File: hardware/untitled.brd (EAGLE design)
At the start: 160 x 100 mm, 39 parts, among them J1 AUDIO_JACK_TRRSSMD_RA, U1 AT32UC3A1512/1256/1128, U2 USD-SOCKETUSD, Y2 CRYSTAL-GROUNDEDSMD-5X3.2

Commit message: PCB updated
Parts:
- added C10, C8: 22 pF, rcl:C0603
- added C22, C9: 33n, rcl:C0402
- added J2: GT-USB-7010, GT-USB-7010:GT-USB-7010
- added R2: 10k, rcl:R0402
- added U$3, U$8: SMT3X6X3.5MM, mw:SMT3X6X3.5MM
- added Y1: CRYSTAL-GROUNDEDSMD-5X3.2, SparkFun-Clocks:CRYSTAL-SMD-5X3.2-4PAD
- C1: device rcl:SMC_B -> rcl:SMC_A
- C2, C3, C4, C5: value (none) -> 2n7
- C6, C7: value (none) -> 33n
- moved C1 79.0 mm to (35.4, 61.2), flipped to the bottom, turned to 90 degrees
- moved R40 75.6 mm to (38.5, 56.9), flipped to the bottom, turned to 90 degrees
- moved R39 68.0 mm to (34.6, 54.1)
- moved R1 67.6 mm to (34.6, 51.1)
- moved R53 66.5 mm to (36.6, 57.0)
- moved C29 64.9 mm to (38.7, 61.4)
- moved U2 64.9 mm to (37.5, 77.5)
- moved C5 64.6 mm to (23.8, 20.3)
- moved C11 64.3 mm to (1.91, 51.4)
- moved C12 64.3 mm to (1.91, 49.5)
- moved C13 64.3 mm to (10.7, 57.8)
- moved C14 64.3 mm to (8.23, 58.1)
- moved C15 64.3 mm to (22.2, 59.3)
- moved C16 64.3 mm to (20.3, 59.5)
- moved C17 64.3 mm to (26.6, 55.5)
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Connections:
- new net D_N: J2.A7, J2.B7, U1.48
- new net D_P: J2.A6, J2.B6, U1.49
- new net KEY_VOLUP: U$8.B, U1.26
- new net OSC_IN: C10.1, U1.85, Y1.1
- new net OSC_OUT: C8.1, U1.86, Y1.3
- new net VBUS: J2.A4B9, J2.B4A9, U1.46
- net 3V: now also R2.2
- net GND: now also C10.2, C22.2, C8.2, C9.2, J2.A1B12, J2.B1A12, U$8.A, U$8.MNT1, U$8.MNT2, Y1.2, Y1.4
- net MOSI: now also R2.1
- net VDDCORE: now also C22.1, C9.1
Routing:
- net 3V: track 48.2 -> 95.8 mm, vias 2 -> 4
- net KEY_VOLUP: track 0.00 -> 29.3 mm
- net OSC_OUT: track 0.00 -> 7.92 mm
- net OSC_IN: track 0.00 -> 7.91 mm
- net I2C1_SDA: track 37.3 -> 30.0 mm
- net I2C1_SCL: track 35.0 -> 28.6 mm
- net D_N: track 0.00 -> 6.07 mm
- net VDDCORE: track 57.1 -> 62.5 mm
- net D_P: track 0.00 -> 5.29 mm
- net GND: track 19.1 -> 23.9 mm
- net N$1: track 25.3 -> 21.2 mm
- net SD_CS: track 32.9 -> 37.0 mm
- net SCK: track 9.99 -> 13.8 mm
- net MISO: track 35.0 -> 34.3 mm
- net SD_PRESENT: track 36.2 -> 36.4 mm, vias 0 -> 1
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- added copper zone on layer 16, net AGND
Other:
- board size 160 x 100 mm -> 47 x 77.8 mm

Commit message: PCB updated
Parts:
- removed J2: GT-USB-7010, GT-USB-7010:GT-USB-7010
- added C27: 2n7, rcl:C0402
- added C28: 33n, rcl:C0402
- added R3, R4, R7: (no value), rcl:R0402
- added U$4: MICRO-USBV2, microusb:MICRO-USB-2
- R15: device rcl:R0603 -> rcl:R0402
- moved C20 1.82 mm to (9.80, 49.0), turned to 180 degrees
- moved R15 0.99 mm to (14.3, 45.6)
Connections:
- new net D_P_1: R7.2, U$4.3
- new net N$4: R4.2, U$4.2
- net 3V: now also C27.1, C28.1, R3.2
- net D_N: now also R4.1; no longer J2.A7, J2.B7
- net D_P: now also R7.1; no longer J2.A6, J2.B6
- net GND: now also C27.2, C28.2, U$4.5, U$4.P$1, U$4.P$2, U$4.P$3, U$4.P$4; no longer J2.A1B12, J2.B1A12
- net I2C1_SDA: now also R3.1
- net VBUS: now also U$4.1; no longer J2.A4B9, J2.B4A9
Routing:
- net VBUS: track 0.00 -> 17.2 mm, vias 0 -> 2
- net GND: track 23.9 -> 27.2 mm, vias 5 -> 7
- net I2C1_SDA: track 30.0 -> 33.1 mm
- net N$4: track 0.00 -> 2.46 mm
- net D_P_1: track 0.00 -> 2.46 mm
- net D_P: track 5.29 -> 6.43 mm
- net D_N: track 6.07 -> 7.20 mm
- net 3V: track 95.8 -> 96.6 mm

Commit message: PCB updated
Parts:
- added C30, C32: 33n, rcl:C0402
- added C31, C33: 100n, rcl:C0402
- C27: value 2n7 -> 33n
- C28: value 33n -> 100n
- moved Y1 3.18 mm to (18.1, 17.4)
- moved C10 3.17 mm to (16.8, 14.0)
- moved C8 3.17 mm to (19.3, 14.0)
- moved R40 0.07 mm to (38.6, 56.9)
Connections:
- net 3V: now also C30.1, C31.1, C32.1, C33.1
- net GND: now also C30.2, C31.2, C32.2, C33.2
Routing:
- net 3V: track 96.6 -> 104.5 mm
- net GND: track 27.2 -> 31.2 mm, vias 7 -> 8
- net OSC_OUT: track 7.92 -> 11.1 mm
- net OSC_IN: track 7.91 -> 11.1 mm
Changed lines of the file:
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@@
 <element name="R39" library="rcl" package="R0603" value="10k" x="34.56" y="54.1274"/>
 <element name="C29" library="rcl" package="C0603" value="100n" x="38.6588" y="61.3664"/>
-<element name="R40" library="rcl" package="R0603" value="10k" x="38.489" y="56.896" rot="MR90"/>
+<element name="R40" library="rcl" package="R0603" value="10k" x="38.5572" y="56.896" rot="MR90"/>
 <element name="C1" library="rcl" package="SMC_A" value="" x="35.3822" y="61.1632" rot="MR90"/>
 <element name="R53" library="rcl" package="R0603" value="10k" x="36.576" y="56.9976" rot="R180"/>
@@
 <element name="C6" library="rcl" package="C0402" value="33n" x="20.955" y="45.8978" rot="R90"/>
 <element name="C7" library="rcl" package="C0402" value="33n" x="25.4" y="44.069" rot="R90"/>
-<element name="C8" library="rcl" package="C0603" value="22 pF" x="19.34845" y="17.145" rot="R270"/>
-<element name="C10" library="rcl" package="C0603" value="22 pF" x="16.80845" y="17.145" rot="R270"/>
-<element name="Y1" library="SparkFun-Clocks" package="CRYSTAL-SMD-5X3.2-4PAD" value="CRYSTAL-GROUNDEDSMD-5X3.2" x="18.07845" y="20.6248"/>
+<element name="C8" library="rcl" package="C0603" value="22 pF" x="19.34845" y="13.97" rot="R270"/>
+<element name="C10" library="rcl" package="C0603" value="22 pF" x="16.80845" y="13.97" rot="R270"/>
+<element name="Y1" library="SparkFun-Clocks" package="CRYSTAL-SMD-5X3.2-4PAD" value="CRYSTAL-GROUNDEDSMD-5X3.2" x="18.07845" y="17.4498"/>
 <element name="C9" library="rcl" package="C0402" value="33n" x="30.4038" y="37.5412"/>
 <element name="C22" library="rcl" package="C0402" value="33n" x="25.146" y="20.32" rot="R270"/>
@@
 <element name="U$4" library="microusb" package="MICRO-USB-2" value="MICRO-USBV2" x="0" y="41.275" rot="R270"/>
 <element name="R7" library="rcl" package="R0402" value="" x="8.255" y="40.9575" rot="R180"/>
-<element name="C27" library="rcl" package="C0402" value="2n7" x="13.1318" y="42.7482" rot="R180"/>
-<element name="C28" library="rcl" package="C0402" value="33n" x="13.1318" y="44.069" rot="R180"/>
+<element name="C27" library="rcl" package="C0402" value="33n" x="13.1318" y="42.7482" rot="R180"/>
+<element name="C28" library="rcl" package="C0402" value="100n" x="13.1318" y="44.069" rot="R180"/>
 <element name="R3" library="rcl" package="R0402" value="" x="15.5702" y="42.7482" rot="R180"/>
+<element name="C30" library="rcl" package="C0402" value="33n" x="15.67688125" y="21.59"/>
+<element name="C31" library="rcl" package="C0402" value="100n" x="15.67688125" y="20.2692"/>
+<element name="C32" library="rcl" package="C0402" value="33n" x="8.89" y="28.450540625" rot="R270"/>
+<element name="C33" library="rcl" package="C0402" value="100n" x="7.5692" y="28.450540625" rot="R270"/>
 </elements>
 <signals>
@@
 <wire x1="5.275" y1="39.975" x2="6.1676" y2="39.975" width="0.4064" layer="1"/>
 <wire x1="6.1676" y1="39.975" x2="6.2484" y2="40.0558" width="0.4064" layer="1"/>
+<contactref element="C30" pad="2"/>
+<contactref element="C31" pad="2"/>
+<wire x1="15.3294" y1="23.8008" x2="15.3294" y2="22.7452" width="0.3048" layer="1"/>
+<wire x1="15.3294" y1="22.7452" x2="15.7988" y2="22.2758" width="0.3048" layer="1"/>
+<wire x1="15.7988" y1="22.2758" x2="16.2814" y2="22.2758" width="0.3048" layer="1"/>
+<wire x1="16.2814" y1="22.2758" x2="16.3068" y2="22.2504" width="0.3048" layer="1"/>
+<via x="14.3256" y="18.4404" extent="1-16" drill="0.6" diameter="1.4224" shape="octagon"/>
+<contactref element="C32" pad="2"/>
+<contactref element="C33" pad="2"/>
+<wire x1="11.3294" y1="28.8008" x2="10.081" y2="28.8008" width="0.3048" layer="1"/>
+<wire x1="10.081" y1="28.8008" x2="9.7028" y2="28.4226" width="0.3048" layer="1"/>
 <wire x1="27.3294" y1="27.8008" x2="27.3294" y2="31.8008" width="0" layer="19" extent="1-1"/>
 <wire x1="27.3294" y1="35.8008" x2="27.3294" y2="31.8008" width="0" layer="19" extent="1-1"/>
-<wire x1="15.3294" y1="23.8008" x2="16.22845" y2="21.7748" width="0" layer="19" extent="1-1"/>
-<wire x1="11.3294" y1="28.8008" x2="15.3294" y2="23.8008" width="0" layer="19" extent="1-1"/>
+<wire x1="9.7028" y1="28.4226" x2="8.89" y2="27.800540625" width="0" layer="19" extent="1-1"/>
 <wire x1="11.3294" y1="32.8008" x2="11.3294" y2="28.8008" width="0" layer="19" extent="1-1"/>
 </signal>
@@
 <wire x1="30.7848" y1="56.8198" x2="33.6282" y2="59.6632" width="0.8128" layer="16"/>
 <wire x1="35.3822" y1="59.6632" x2="33.6282" y2="59.6632" width="0.8128" layer="16"/>
-<wire x1="38.489" y1="57.746" x2="38.489" y2="58.7392" width="0.6096" layer="16"/>
-<wire x1="38.489" y1="58.7392" x2="37.5666" y2="59.6616" width="0.6096" layer="16"/>
 <contactref element="C27" pad="1"/>
 <contactref element="U1" pad="68"/>
@@
 <wire x1="13.7818" y1="42.7482" x2="14.9202" y2="42.7482" width="0.6096" layer="1"/>
 <wire x1="14.8294" y1="42.6574" x2="14.9202" y2="42.7482" width="0.3048" layer="1"/>
+<contactref element="C31" pad="1"/>
+<contactref element="C30" pad="1"/>
+<wire x1="14.8294" y1="23.8008" x2="14.8294" y2="21.59" width="0.3048" layer="1"/>
+<wire x1="14.8294" y1="21.59" x2="14.8294" y2="20.46668125" width="0.3048" layer="1"/>
+<wire x1="14.8294" y1="20.46668125" x2="15.02688125" y2="20.2692" width="0.3048" layer="1"/>
+<wire x1="15.02688125" y1="21.59" x2="14.8294" y2="21.59" width="0.3048" layer="1"/>
+<contactref element="C33" pad="1"/>
+<contactref element="C32" pad="1"/>
+<wire x1="11.3294" y1="29.3008" x2="8.89" y2="29.3008" width="0.3048" layer="1"/>
+<wire x1="8.89" y1="29.3008" x2="7.769459375" y2="29.3008" width="0.3048" layer="1"/>
+<wire x1="7.769459375" y1="29.3008" x2="7.5692" y2="29.100540625" width="0.3048" layer="1"/>
+<wire x1="8.89" y1="29.100540625" x2="8.89" y2="29.3008" width="0.3048" layer="1"/>
+<wire x1="38.5572" y1="57.746" x2="38.5572" y2="58.671" width="0.6096" layer="16"/>
+<wire x1="38.5572" y1="58.671" x2="37.5666" y2="59.6616" width="0.6096" layer="16"/>
 <wire x1="27.3294" y1="27.3008" x2="27.3294" y2="31.3008" width="0" layer="19" extent="1-1"/>
 <wire x1="33.02" y1="31.3008" x2="27.3294" y2="31.3008" width="0" layer="19" extent="1-1"/>
@@
 <wire x1="23.3294" y1="40.9316" x2="23.749" y2="41.3512" width="0.3048" layer="1"/>
 <wire x1="23.749" y1="41.3512" x2="29.0322" y2="41.3512" width="0.3048" layer="1"/>
-<via x="38.489" y="54.48" extent="1-16" drill="0.6" diameter="1.27" shape="octagon"/>
-<wire x1="29.0322" y1="41.3512" x2="38.489" y2="50.808" width="0.3048" layer="1"/>
-<wire x1="38.489" y1="54.48" x2="38.489" y2="50.808" width="0.3048" layer="1"/>
-<wire x1="38.489" y1="54.48" x2="38.489" y2="57.1834" width="0.3048" layer="1"/>
+<via x="38.5572" y="54.48" extent="1-16" drill="0.6" diameter="1.27" shape="octagon"/>
+<wire x1="29.0322" y1="41.3512" x2="38.5572" y2="50.8762" width="0.3048" layer="1"/>
 <wire x1="43.315" y1="63.22" x2="43.315" y2="62.0094" width="0.3048" layer="1"/>
-<wire x1="43.315" y1="62.0094" x2="38.489" y2="57.1834" width="0.3048" layer="1"/>
-<wire x1="38.489" y1="56.046" x2="38.489" y2="54.48" width="0.6096" layer="16"/>
+<wire x1="43.315" y1="62.0094" x2="38.5572" y2="57.2516" width="0.3048" layer="1"/>
+<wire x1="38.5572" y1="50.8762" x2="38.5572" y2="54.48" width="0.3048" layer="1"/>
+<wire x1="38.5572" y1="54.48" x2="38.5572" y2="57.2516" width="0.3048" layer="1"/>
+<wire x1="38.5572" y1="54.48" x2="38.5572" y2="56.046" width="0.6096" layer="16"/>
 </signal>
 <signal name="N$1">
@@
 <contactref element="Y1" pad="3"/>
 <contactref element="U1" pad="86"/>
-<wire x1="18.3294" y1="23.8008" x2="18.3294" y2="21.7748" width="0.3048" layer="1"/>
-<wire x1="18.3294" y1="21.7748" x2="18.3294" y2="18.8562" width="0.3048" layer="1"/>
-<wire x1="19.92845" y1="21.7748" x2="18.3294" y2="21.7748" width="0.3048" layer="1"/>
-<wire x1="18.3294" y1="18.8562" x2="19.1906" y2="17.995" width="0.3048" layer="1"/>
-<wire x1="19.34845" y1="17.995" x2="19.1906" y2="17.995" width="0.3048" layer="1"/>
+<wire x1="18.3294" y1="23.8008" x2="18.3294" y2="18.5998" width="0.3048" layer="1"/>
+<wire x1="18.3294" y1="18.5998" x2="18.3294" y2="15.6812" width="0.3048" layer="1"/>
+<wire x1="19.92845" y1="18.5998" x2="18.3294" y2="18.5998" width="0.3048" layer="1"/>
+<wire x1="18.3294" y1="15.6812" x2="19.1906" y2="14.82" width="0.3048" layer="1"/>
+<wire x1="19.34845" y1="14.82" x2="19.1906" y2="14.82" width="0.3048" layer="1"/>
 </signal>
 <signal name="OSC_IN">
@@
 <contactref element="Y1" pad="1"/>
 <contactref element="U1" pad="85"/>
-<wire x1="17.8294" y1="23.8008" x2="17.8294" y2="19.4748" width="0.3048" layer="1"/>
-<wire x1="17.8294" y1="19.4748" x2="17.8294" y2="18.8708" width="0.3048" layer="1"/>
-<wire x1="16.22845" y1="19.4748" x2="17.8294" y2="19.4748" width="0.3048" layer="1"/>
-<wire x1="17.8294" y1="18.8708" x2="16.9536" y2="17.995" width="0.3048" layer="1"/>
-<wire x1="16.80845" y1="17.995" x2="16.9536" y2="17.995" width="0.3048" layer="1"/>
+<wire x1="17.8294" y1="23.8008" x2="17.8294" y2="16.2998" width="0.3048" layer="1"/>
+<wire x1="17.8294" y1="16.2998" x2="17.8294" y2="15.6958" width="0.3048" layer="1"/>
+<wire x1="16.22845" y1="16.2998" x2="17.8294" y2="16.2998" width="0.3048" layer="1"/>
+<wire x1="17.8294" y1="15.6958" x2="16.9536" y2="14.82" width="0.3048" layer="1"/>
+<wire x1="16.80845" y1="14.82" x2="16.9536" y2="14.82" width="0.3048" layer="1"/>
 </signal>
 <signal name="KEY_VOLUP">

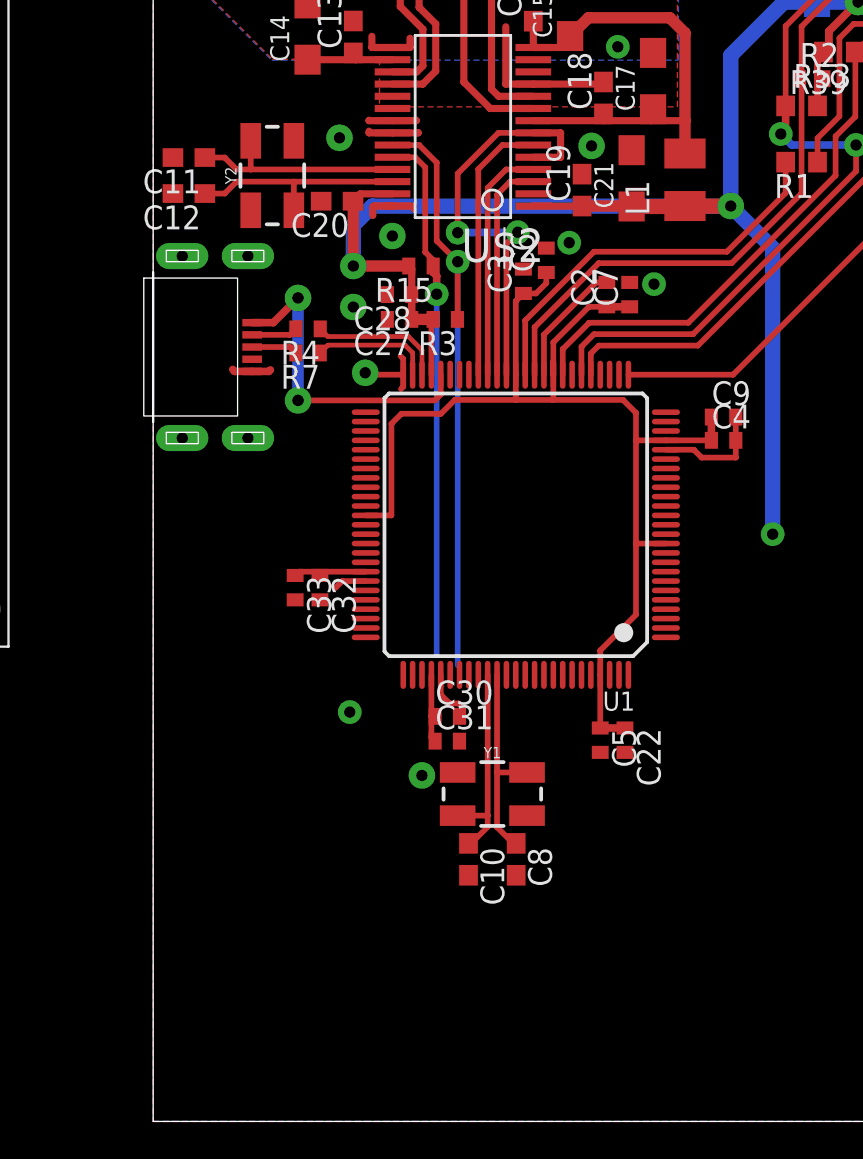
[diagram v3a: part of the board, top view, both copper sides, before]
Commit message: PCB update. USB-C instead of microUSB, PMIC (work in progress)
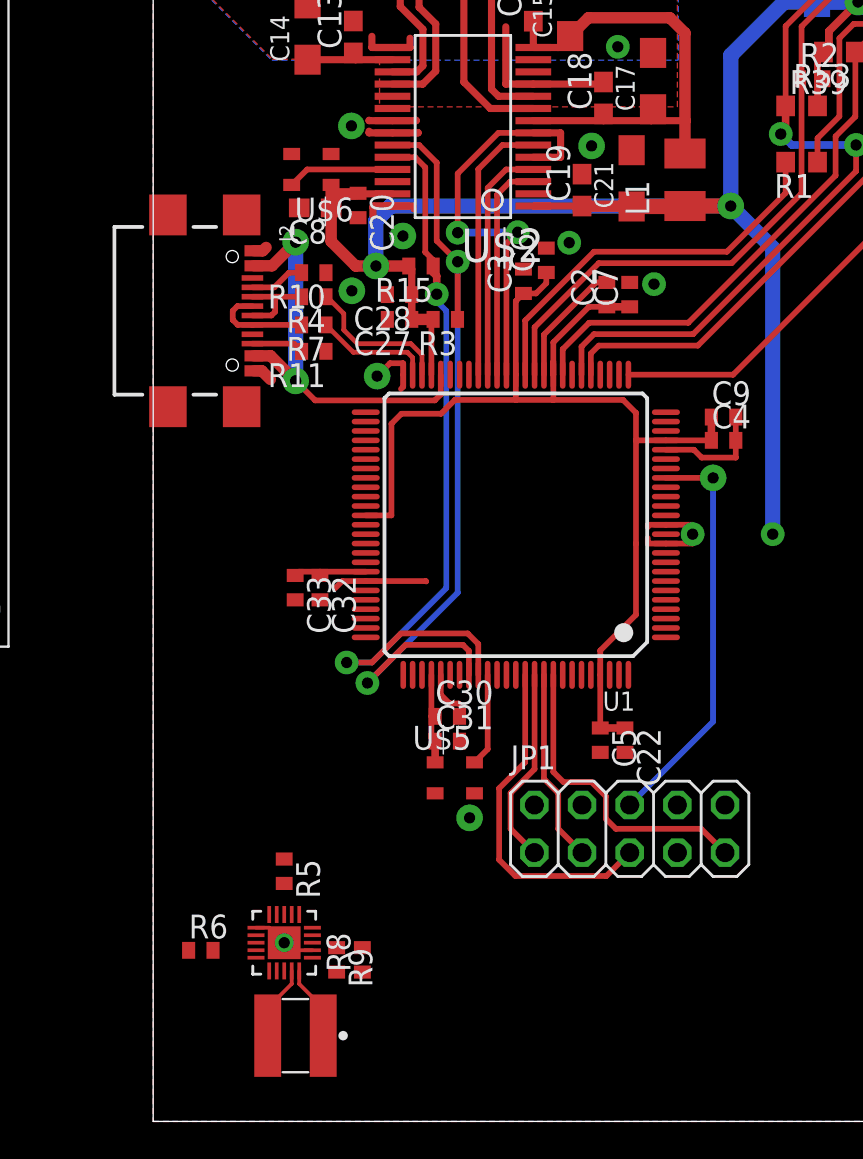
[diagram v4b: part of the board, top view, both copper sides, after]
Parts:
- removed C10, C11, C12: 22 pF, rcl:C0603
- removed U$4: MICRO-USBV2, microusb:MICRO-USB-2
- removed Y1, Y2: CRYSTAL-GROUNDEDSMD-5X3.2, SparkFun-Clocks:CRYSTAL-SMD-5X3.2-4PAD
- added J2: USB4110-GF-A, connector_tst:GCT_USB4110-GF-A
- added JP1: (no value), pinhead:2X05
- added L2: COILCRAFT-LPS4018, passives:LPS4018
- added R10, R11, R5, R6, R8, R9: (no value), rcl:R0402
- added U$5, U$6: ASE, crystal:ASE
- added U3: LTC3558EUDTRPBFQFN-20_UD_LIT-M, mw:QFN-20_UD_LIT-M
- C20: device rcl:C0603 -> rcl:C0402
- C8: value 22 pF -> (none)
- moved C8 36.3 mm to (8.64, 48.7), turned to 180 degrees
- moved R4 1.74 mm to (8.56, 44.0)
- moved R7 1.53 mm to (8.56, 42.5)
- moved C20 1.14 mm to (10.9, 48.8), turned to 270 degrees
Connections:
- removed net D_P_1: R7.2, U$4.3
- removed net N$4: R4.2, U$4.2
- removed net XTI: C11.1, U$2.P$25, Y2.3
- removed net XTO: C12.1, U$2.P$26, Y2.1
- new net /RESET: JP1.6, U1.18
- new net D2_N: J2.A7, J2.B7, R4.2
- new net D2_P: J2.A6, J2.B6, R7.2
- new net MCLK: U$2.P$25, U$6.3
- new net N$10: JP1.8
- new net N$2: L2.2, U3.9
- new net N$3: L2.1, U3.10
- new net N$5: R5.2, U3.18
- new net N$6: R6.2, U3.4
- new net N$7: R8.2, R9.1, U3.13
- new net N$8: J2.B5, R11.2
- new net N$9: J2.A5, R10.2
- new net TCK: JP1.1, U1.90
- new net TDI: JP1.9, U1.92
- new net TDO: JP1.3, U1.91
- new net TMS: JP1.5, U1.89
- net 3V: now also C8.1, JP1.4, R9.2, U$5.4, U$6.4, U3.11; no longer U1.12
- net GND: now also J2.A1/B12, J2.B1/A12, J2.S1, J2.S2, J2.S3, J2.S4, JP1.10, JP1.2, R10.1, R11.1, R5.1, R6.1, R8.1, U$5.2, U$6.2, U1.11, U1.12, U3.1, U3.12; no longer C10.2, C11.2, C12.2, U$4.5, U$4.P$1, U$4.P$2, U$4.P$3, U$4.P$4, Y1.2, Y1.4, Y2.2, Y2.4
- net OSC_IN: now also U$5.3; no longer C10.1, Y1.1
- net OSC_OUT: no longer C8.1, Y1.3
- net VBUS: now also J2.A4/B9, J2.B4/A9, U3.20; no longer U$4.1
- net VDDCORE: no longer U1.11
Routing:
- net /RESET: track 0.00 -> 21.8 mm, vias 0 -> 1
- net TMS: track 0.00 -> 18.3 mm
- net TDI: track 0.00 -> 16.8 mm
- net I2C1_SCL: track 28.2 -> 41.3 mm, vias 1 -> 2
- net GND: track 31.2 -> 43.0 mm, vias 8 -> 10
- net XTO: track 11.8 -> 0.00 mm
- net XTI: track 11.8 -> 0.00 mm
- net OSC_OUT: track 11.1 -> 0.00 mm
- net I2C1_SDA: track 33.1 -> 43.7 mm
- net TCK: track 0.00 -> 10.5 mm
- net TDO: track 0.00 -> 10.3 mm
- net OSC_IN: track 11.1 -> 4.95 mm
- net MCLK: track 0.00 -> 5.72 mm
- net D2_P: track 0.00 -> 5.41 mm
- net VBUS: track 17.2 -> 22.3 mm
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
